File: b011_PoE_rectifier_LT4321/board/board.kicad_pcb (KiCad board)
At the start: 2 copper layers, 21 x 29 mm, 11 parts, among them J1 004_BASE-T_CT_2x3, J2 PoE_2x2, Q1 PSMN040-100MSEX, Q2 PSMN040-100MSEX, Q3 PSMN040-100MSEX, Q4 PSMN040-100MSEX, Q5 PSMN040-100MSEX, Q6 PSMN040-100MSEX, Q7 PSMN040-100MSEX, Q8 PSMN040-100MSEX, U1 LT4321

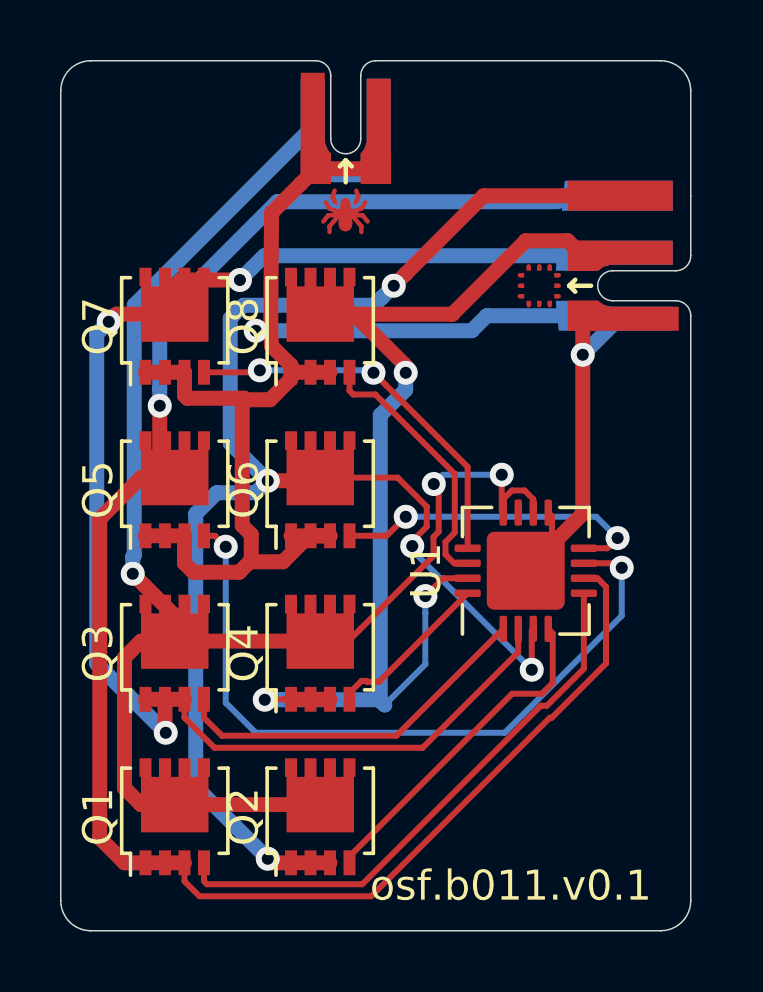
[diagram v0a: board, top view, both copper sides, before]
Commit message: cleaned up symbol lib paths
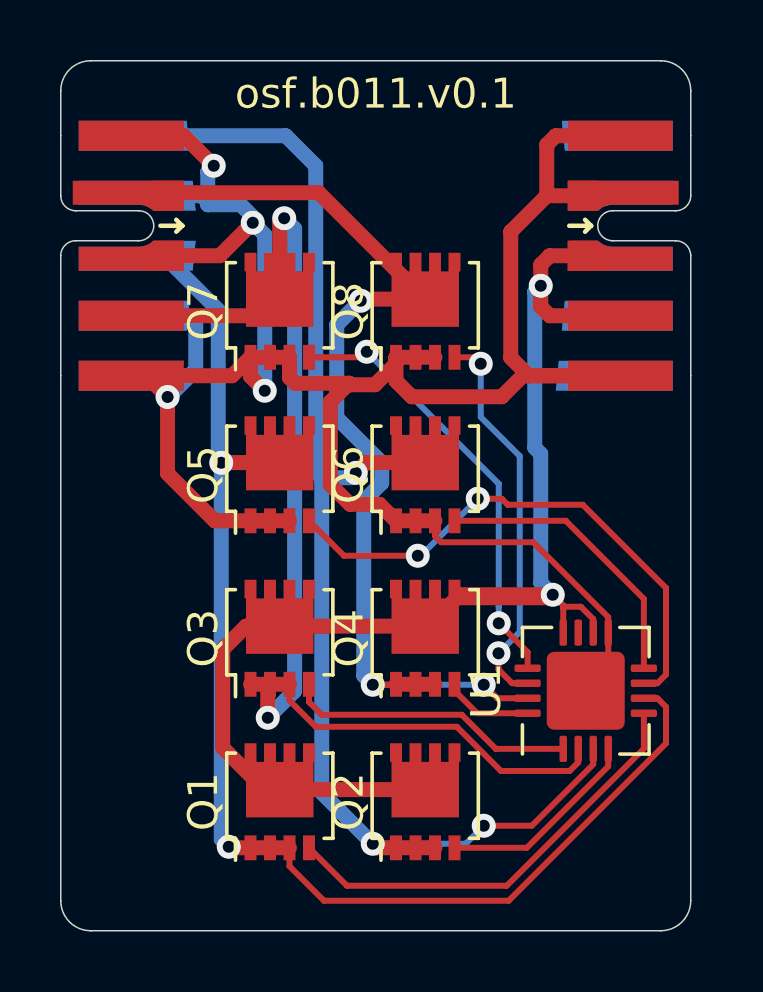
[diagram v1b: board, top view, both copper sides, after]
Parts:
- J1: footprint on_edge:on_edge_2x03_device -> on_edge:on_edge_2x05_device
- J2: footprint on_edge:on_edge_2x02_host -> on_edge:on_edge_2x05_host
- moved J1 21.0 mm to (120.0, 86.5), turned to 270 degrees
- moved J2 12.3 mm to (141.0, 86.5), turned to 270 degrees
- moved U1 4.47 mm to (137.5, 101.0)
- moved Q1 3.54 mm to (127.3, 104.7)
- moved Q2 3.54 mm to (132.2, 104.7)
- moved Q3 3.54 mm to (127.3, 99.2)
- moved Q4 3.54 mm to (132.2, 99.2)
- moved Q5 3.54 mm to (127.3, 93.8)
- moved Q6 3.54 mm to (132.2, 93.8)
- moved Q7 3.54 mm to (127.3, 88.3)
- moved Q8 3.54 mm to (132.2, 88.3)
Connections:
- J1 pad 5: /snippet/CT3 -> GND
- J1 pad 6: /snippet/CT4 -> /snippet/CT3
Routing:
- net GND: track 58.6 -> 90.0 mm, vias 2 -> 4
- net /snippet/CT4: track 60.9 -> 44.9 mm, vias 1 -> 2
- net /snippet/P: track 56.2 -> 46.2 mm, vias 3 -> 2
- net /snippet/CT3: track 52.5 -> 44.7 mm, vias 5 -> 3
- net /snippet/CT2: track 50.2 -> 42.9 mm, vias 3 -> 2
- net /snippet/BG_78: track 24.2 -> 18.1 mm
- net /snippet/TG_45: track 11.2 -> 6.83 mm
- net /snippet/BG_12: track 8.95 -> 13.1 mm, vias 0 -> 2
- net /snippet/TG_78: track 18.8 -> 14.8 mm
- net /snippet/CT1: track 37.5 -> 33.8 mm
- net /snippet/TG_36: track 12.3 -> 9.71 mm
- net /snippet/TG_12: track 5.55 -> 2.96 mm
- net /snippet/BG_36: track 12.9 -> 14.8 mm
- net /snippet/BG_45: track 10.8 -> 9.70 mm, vias 2 -> 0
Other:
- outline, holes or cut-outs redrawn

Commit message: changed mosfet for availability
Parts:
- added LOGO1: Logo_Open_Hardware_Small, Symbol:OSHW-Logo2_9.8x8mm_SilkScreen, B.Cu at (125.5, 104.5)
- J2: value PoE_2x2 -> 013_PoE_rectified
- Q1, Q2, Q3, Q4, Q5, Q6, Q7, Q8: value PSMN040-100MSEX -> TPN3300ANH,LQ
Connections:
- U1 pad 11: (no net) -> /snippet/PWRGD
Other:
- board text added: "osf.004.v1.0"
- board text added: "osf.013.v1.0"
- board text added: "osf.b011.v0.2"
- board text removed: "osf.b011.v0.1"

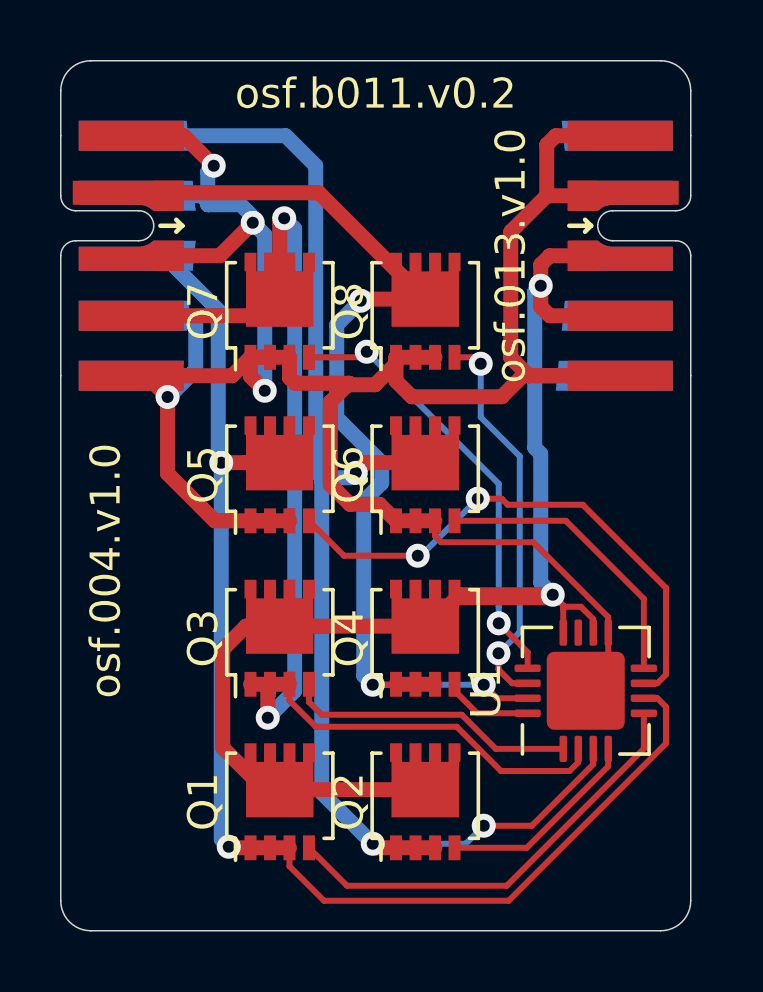
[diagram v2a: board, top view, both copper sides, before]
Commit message: updated to kicad 6
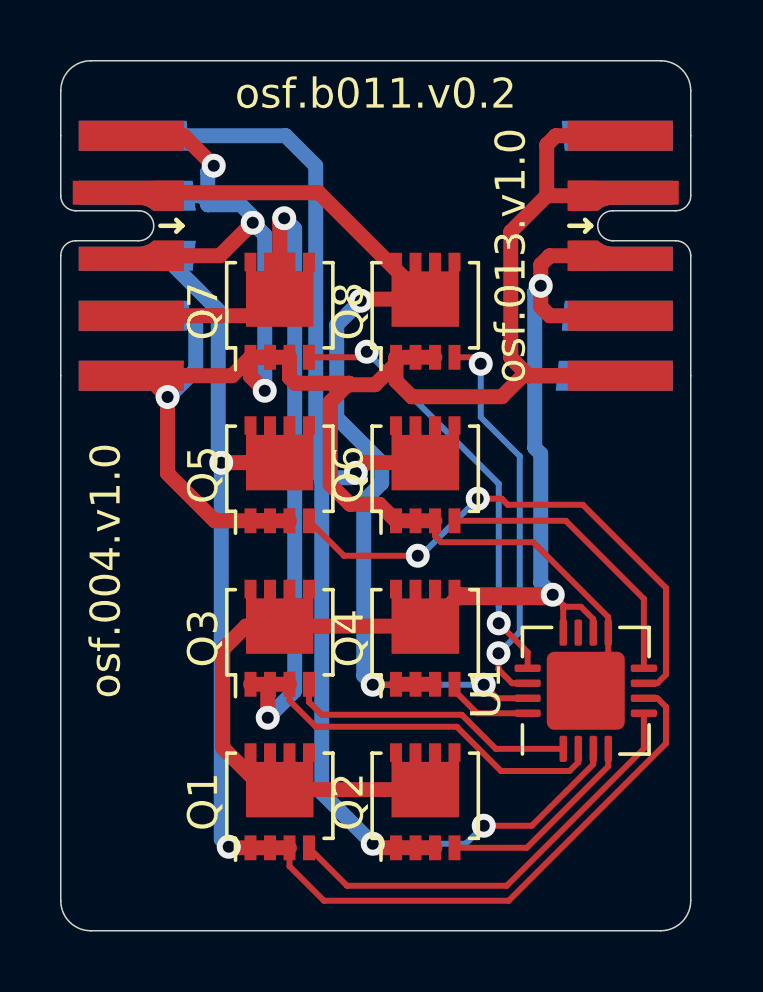
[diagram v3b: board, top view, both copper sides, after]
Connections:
- net /snippet/CT1 renamed /snippet/CT_12
- net /snippet/CT2 renamed /snippet/CT_36
- net /snippet/CT3 renamed /snippet/CT_45
- net /snippet/CT4 renamed /snippet/CT_78
- net /snippet/P renamed /snippet/VPORTP
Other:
- net class Default removed
